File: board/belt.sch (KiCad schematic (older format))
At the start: 21 parts, among them J1 USB_B_Micro, J2 USB_B_Micro, J3 USB_B_Micro, J4 USB_B_Micro, P1 3352T-1-103LF, Q1 BSS138, Q2 BSS138, SW1 SW_DPDT, SW2 SW_Push, U1 Teensy4.0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

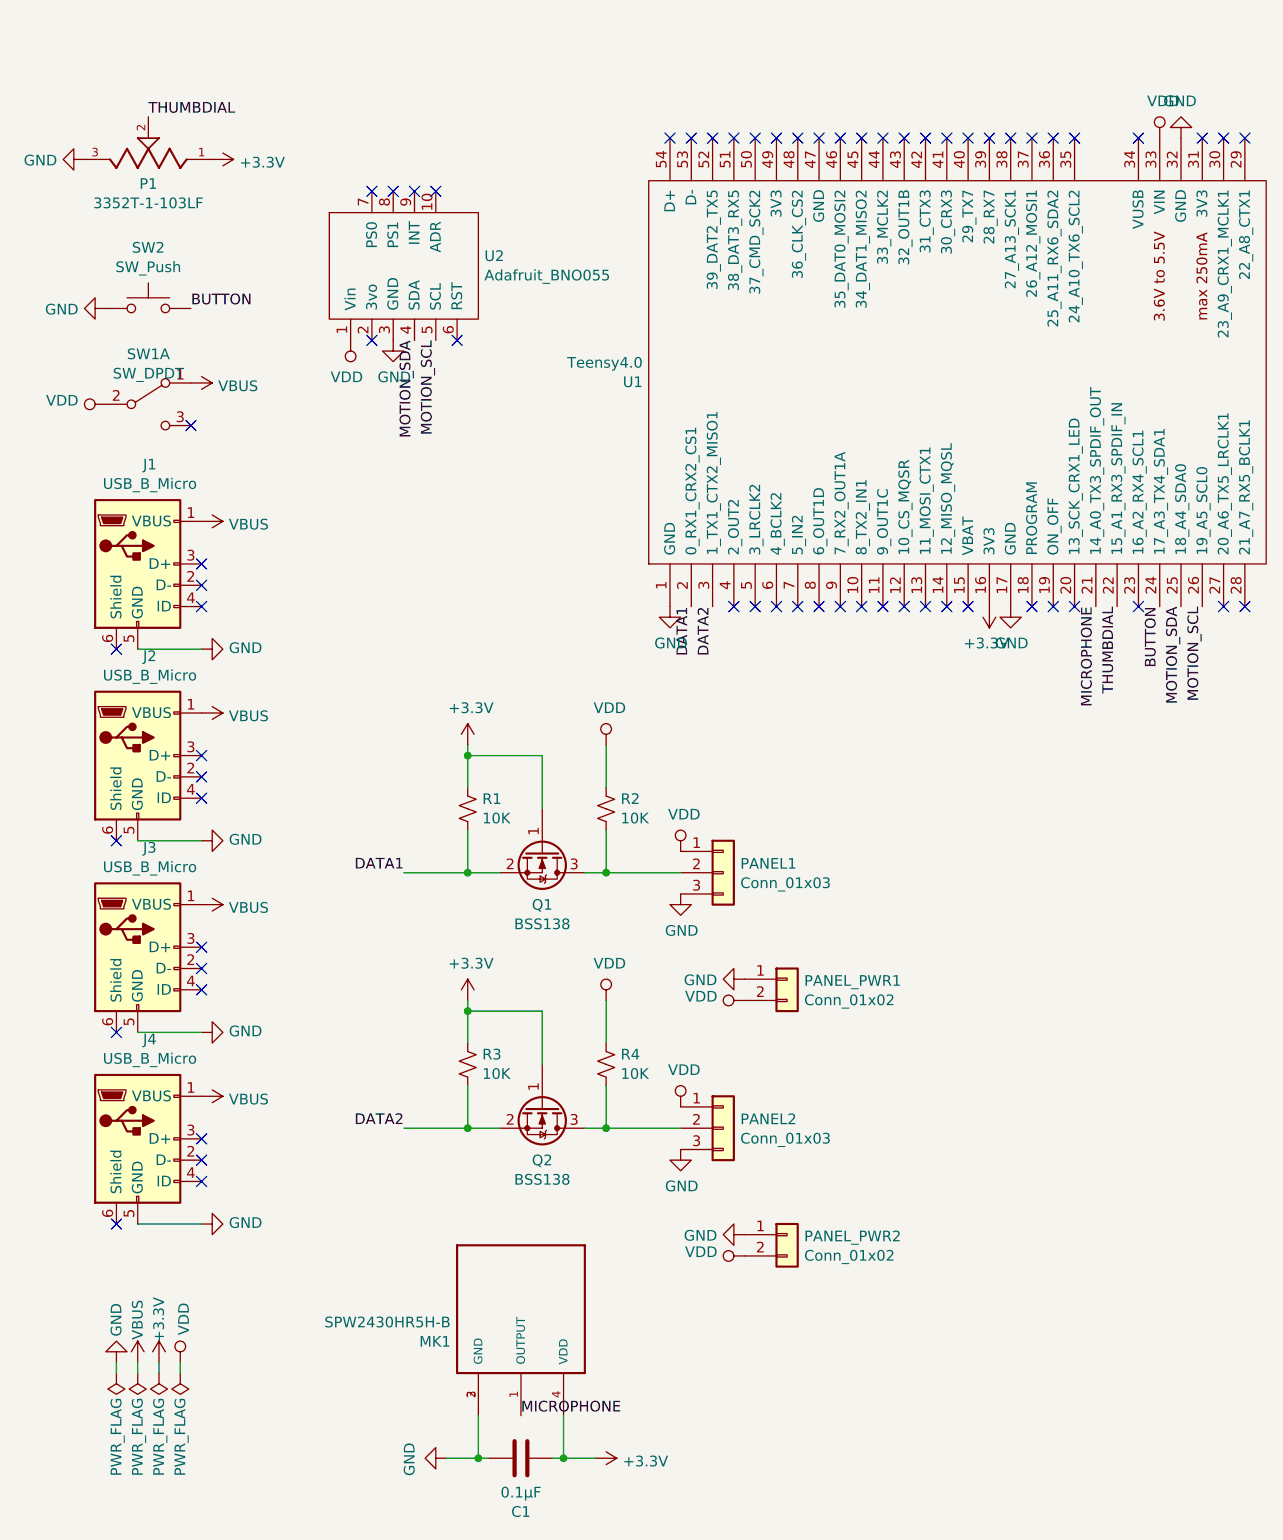
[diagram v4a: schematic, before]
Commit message: checkpoint for 3rd board layout with veritcal structure, two pots, and digital mic
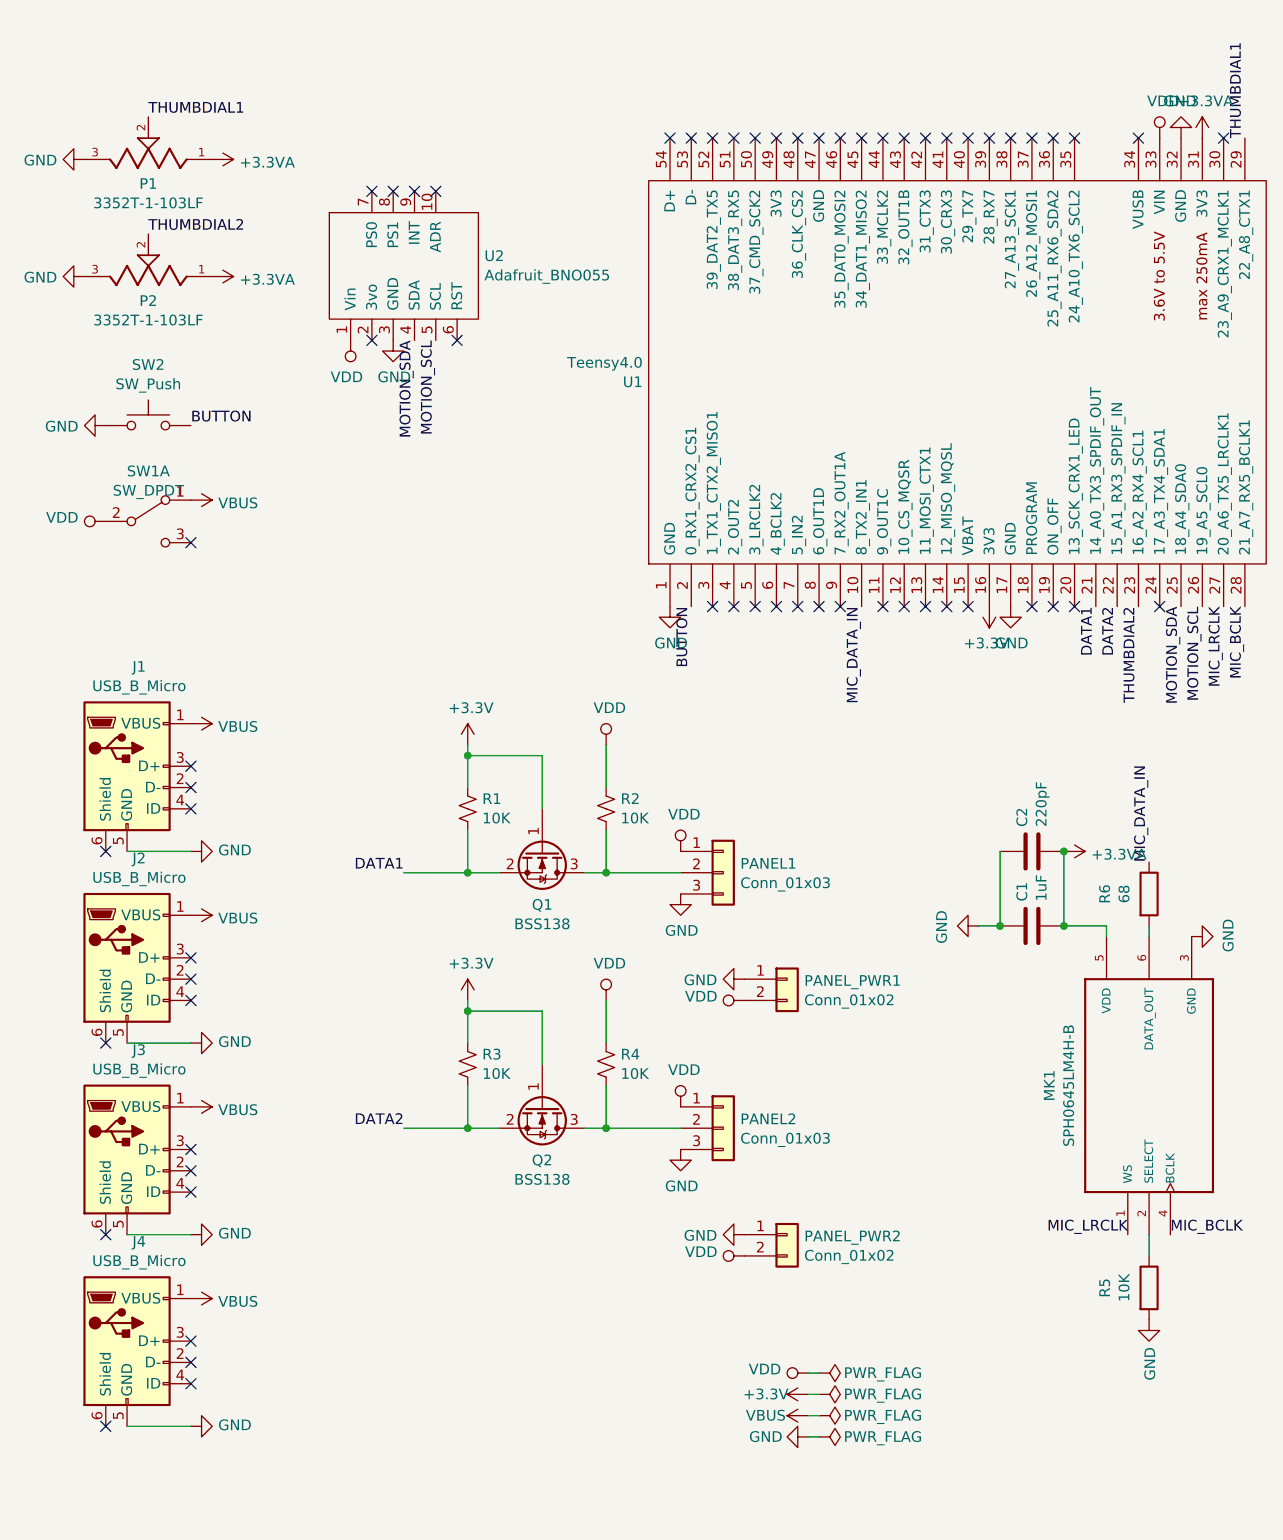
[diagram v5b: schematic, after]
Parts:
- removed MK1: SPW2430HR5H-B, SPW2430HR5H-B:MIC_SPW2430HR5H-B, symbol MIC_SPW2430HR5H-B:SPW2430HR5H-B
- added C2: 220pF, Capacitor_SMD:C_0805_2012Metric, symbol Device:C
- added MK1: SPH0645LM4H-B, Mic-SPH0645LM4H-B:MIC_SPH0645LM4H-B, symbol Mic_I2S_SPH0645LM4H-B:SPH0645LM4H-B
- added P2: 3352T-1-103LF, Potentiometer_THT:PDB12-H, symbol belt-rescue:3352T-1-103LF-3352T-1-103LF
- added R5: 10K, Resistor_SMD:R_0805_2012Metric, symbol Device:R
- added R6: 68, Resistor_SMD:R_0805_2012Metric, symbol Device:R
- C1: value 0.1µF -> 1uF
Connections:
- net MICROPHONE is gone; now on net DATA1: U1.21 (14_A0_TX3_SPDIF_OUT)
- net +3V3: no longer C1.1, P1.1 (CCW)
- net BUTTON: now also U1.2 (0_RX1_CRX2_CS1); no longer U1.24 (17_A3_TX4_SDA1)
- net DATA1: no longer U1.2 (0_RX1_CRX2_CS1)
- net DATA2: now also U1.22 (15_A1_RX3_SPDIF_IN); no longer U1.3 (1_TX1_CTX2_MISO1)
- net GND: now also C1.1, C2.1, MK1.3 (GND), P2.3 (CW), R5.2; no longer C1.2
- net MIC_DATA_IN: now reaches U1.10 (8_TX2_IN1)
- net MIC_DATA_IN: now also R6.1
- net THUMBDIAL2: now reaches U1.23 (16_A2_RX4_SCL1)
- net THUMBDIAL2: now also P2.2 (WIPER)
- net MIC_LRCLK: now reaches U1.27 (20_A6_TX5_LRCLK1)
- net MIC_LRCLK: now also MK1.1 (WS)
- net MIC_BCLK: now reaches U1.28 (21_A7_RX5_BCLK1)
- net MIC_BCLK: now also MK1.4 (BCLK)
- net THUMBDIAL1: now reaches U1.29 (22_A8_CTX1)
- net THUMBDIAL1: now also P1.2 (WIPER)
- net +3.3VA: now reaches U1.31 (3V3)
- net +3.3VA: now also C1.2, P1.1 (CCW), C2.2, MK1.5 (VDD), P2.1 (CCW)
- removed net THUMBDIAL: P1.2 (WIPER), U1.22 (15_A1_RX3_SPDIF_IN)
- new net: MK1.2 (SELECT), R5.1
- new net: MK1.6 (DATA_OUT), R6.2
- no-connect marks 65 -> 61
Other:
- moved on the sheet: J1, J2, J3, J4, SW1A, SW2

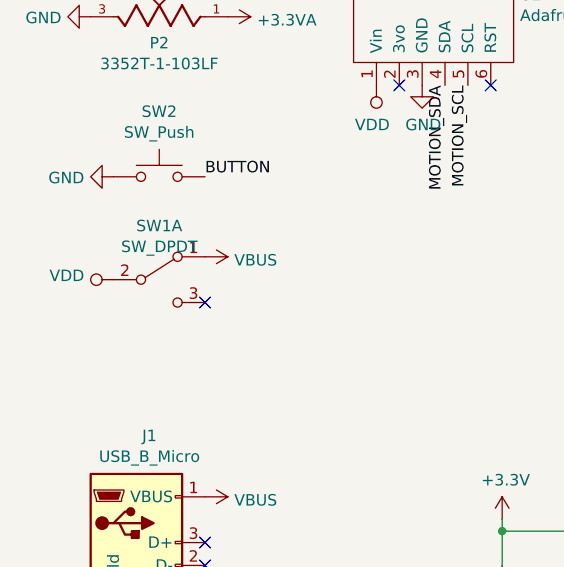
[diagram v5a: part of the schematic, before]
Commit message: new placement for led pads plus a strategy for securing them; tweaks; nearing final design
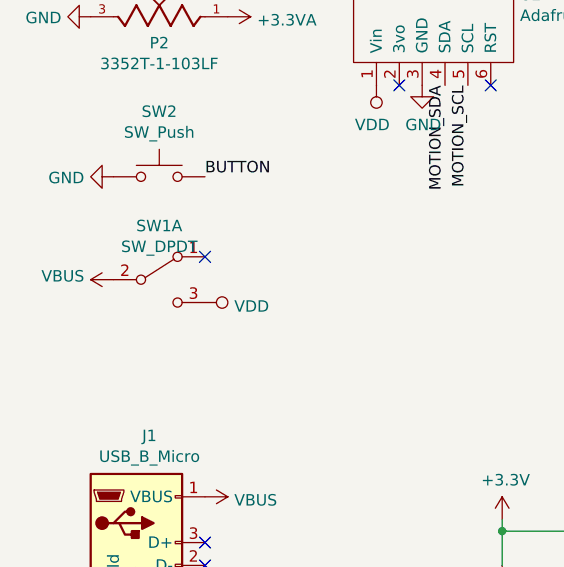
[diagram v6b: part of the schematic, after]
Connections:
- net VBUS: now also SW1.2 (B); no longer SW1.1 (A)
- net VDD: now also SW1.3 (C); no longer SW1.2 (B)
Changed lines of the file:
@@
 L power:VDD #PWR0120
 U 1 1 5E3ACFA6
+P 1700 2850
+F 0 "#PWR0120" H 1700 2700 50  0001 C CNN
+F 1 "VDD" V 1717 2978 50  0000 L CNN
+F 2 "" H 1700 2850 50  0001 C CNN
+F 3 "" H 1700 2850 50  0001 C CNN
+	1    1700 2850
+	0    1    1    0
+$EndComp
+$Comp
+L power:VBUS #PWR0111
+U 1 1 5E3E2BC8
 P 1300 2750
-F 0 "#PWR0120" H 1300 2600 50  0001 C CNN
-F 1 "VDD" V 1317 2878 50  0000 L CNN
+F 0 "#PWR0111" H 1300 2600 50  0001 C CNN
+F 1 "VBUS" V 1315 2878 50  0000 L CNN
 F 2 "" H 1300 2750 50  0001 C CNN
 F 3 "" H 1300 2750 50  0001 C CNN
 	1    1300 2750
 	0    -1   -1   0
-$EndComp
-$Comp
-L power:VBUS #PWR0111
-U 1 1 5E3E2BC8
-P 1700 2650
-F 0 "#PWR0111" H 1700 2500 50  0001 C CNN
-F 1 "VBUS" V 1715 2778 50  0000 L CNN
-F 2 "" H 1700 2650 50  0001 C CNN
-F 3 "" H 1700 2650 50  0001 C CNN
-	1    1700 2650
-	0    1    1    0
 $EndComp
 $Comp
@@
 $EndComp
 NoConn ~ 4250 3150
-NoConn ~ 1700 2850
+NoConn ~ 1700 2650
 $Comp
 L belt-rescue:3352T-1-103LF-3352T-1-103LF P2

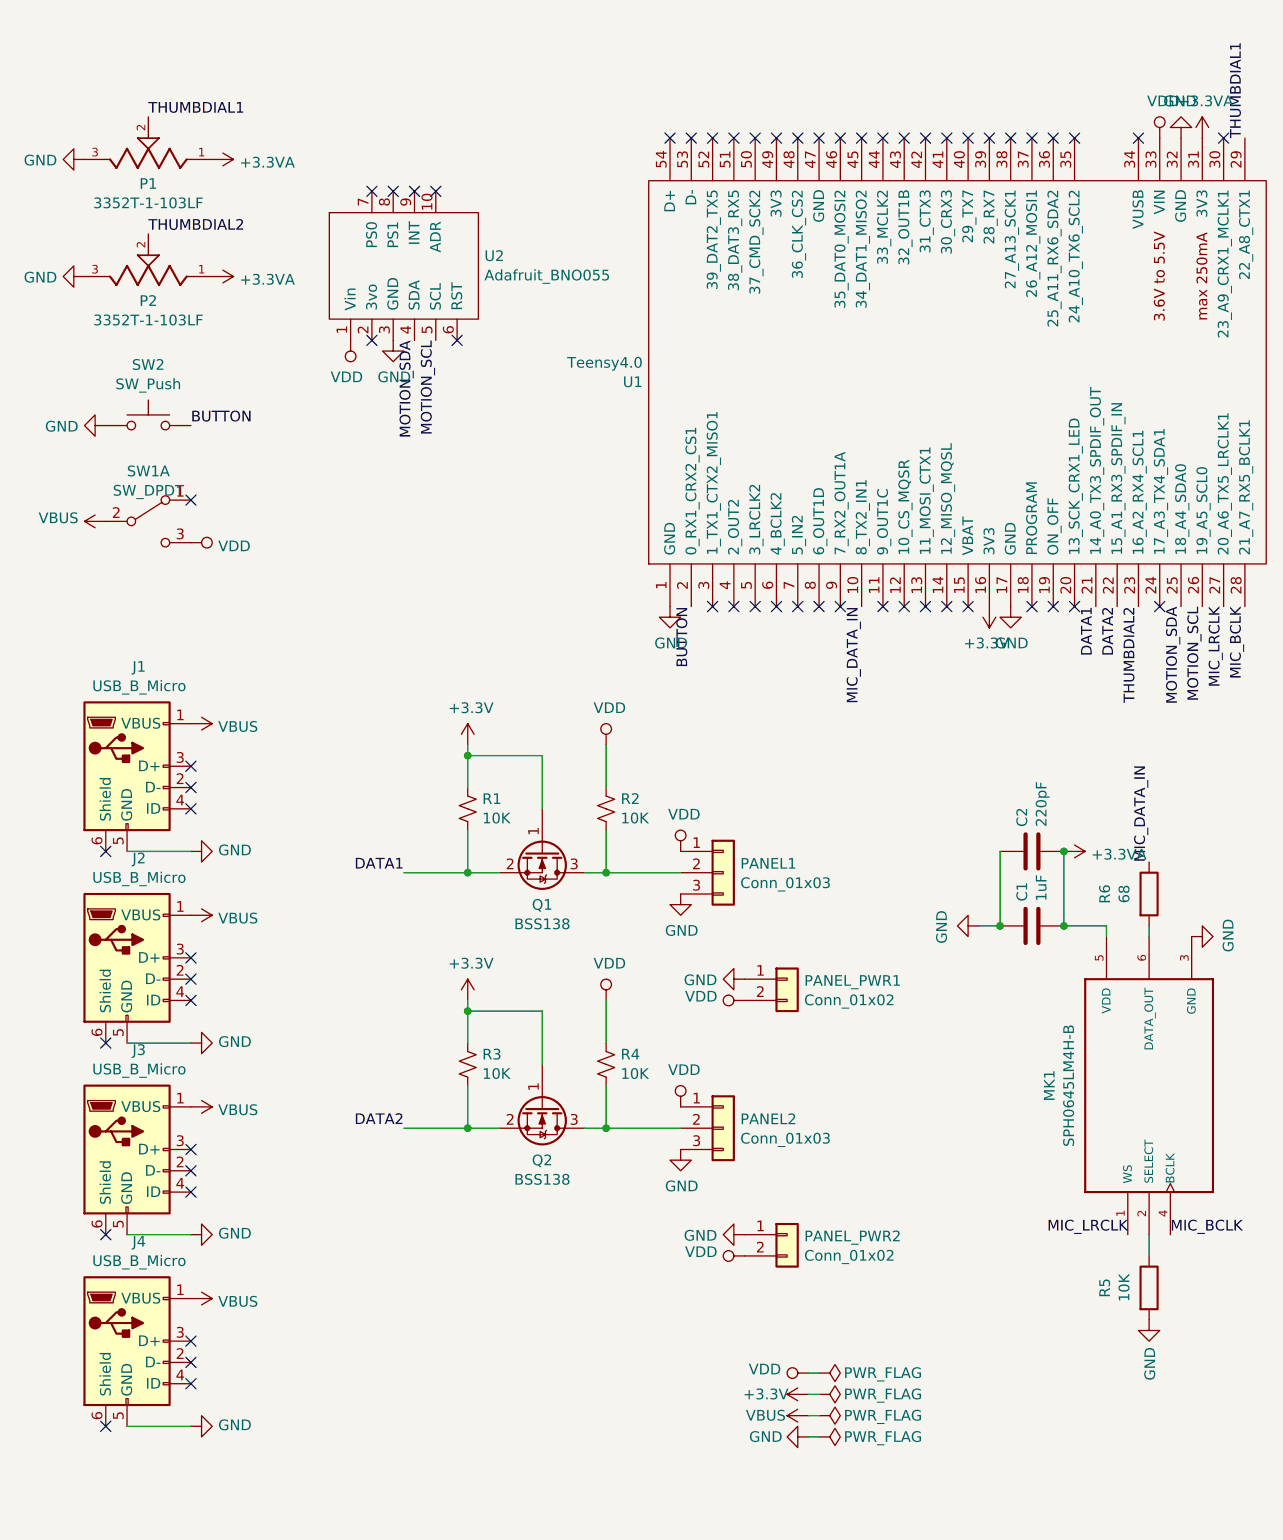
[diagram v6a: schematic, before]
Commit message: digikey was out of the DPDT switch I was going to use, so replace with a smaller (better?) one; shrink board vertically slightly in response
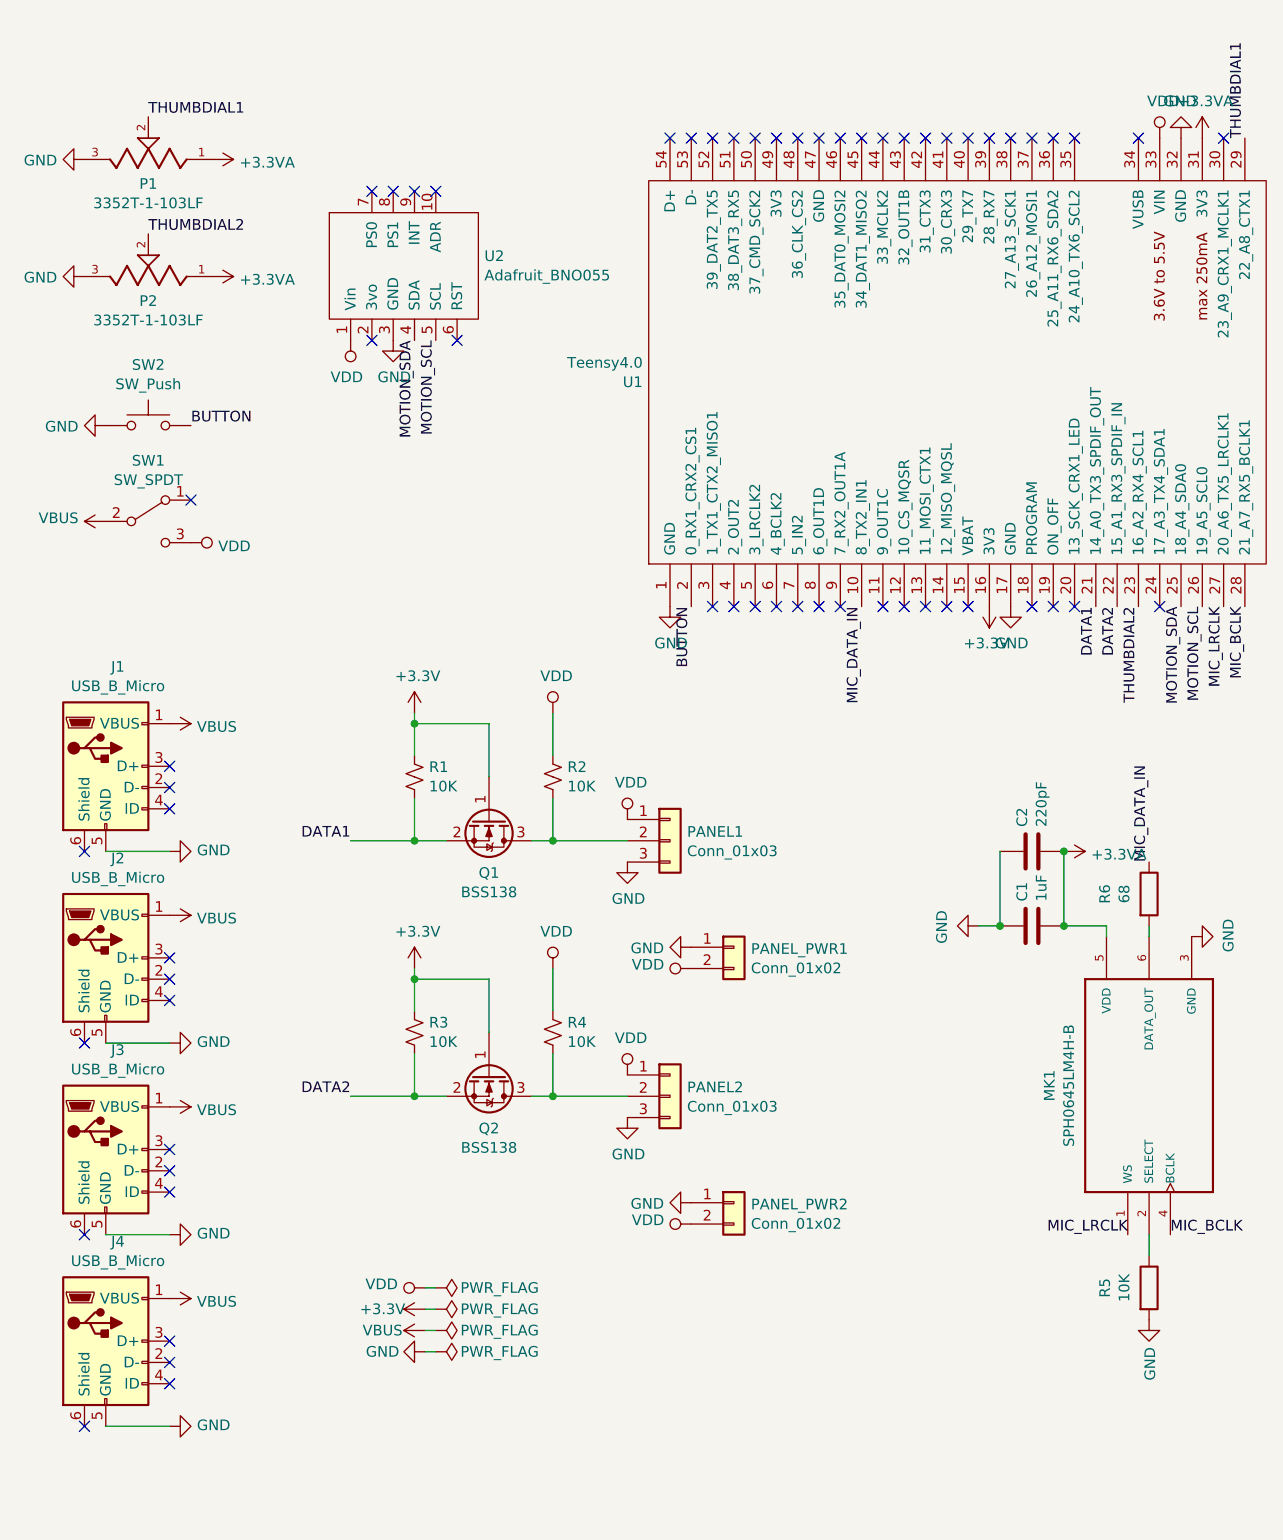
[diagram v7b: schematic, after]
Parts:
- removed SW1: SW_DPDT, engstad:slide-switch-MFS201N-9-Z, symbol Switch:SW_DPDT_x2
- added SW1: SW_SPDT, Extra SMD Components:Button_Switch_SPDT_GH36P010001, symbol Switch:SW_SPDT
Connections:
- net VBUS: now also SW1.2 (B)
- net VDD: now also SW1.3 (C)
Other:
- moved on the sheet: J1, J2, J3, J4, PANEL1, PANEL2, PANEL_PWR1, PANEL_PWR2, Q1, Q2, R1, R2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

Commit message: switch 10K resistors to 0603 package (being ambitious and buying in bulk); fix layout for new package
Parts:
- R1, R2, R3, R4, R5: footprint Resistor_SMD:R_0805_2012Metric -> Resistor_SMD:R_0603_1608Metric
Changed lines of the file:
@@
 F 0 "R1" H 2818 3996 50  0000 L CNN
 F 1 "10K" H 2818 3905 50  0000 L CNN
-F 2 "Resistor_SMD:R_0805_2012Metric" H 2750 3950 50  0001 C CNN
+F 2 "Resistor_SMD:R_0603_1608Metric" H 2750 3950 50  0001 C CNN
 F 3 "~" H 2750 3950 50  0001 C CNN
 	1    2750 3950
@@
 F 0 "R3" H 2818 5196 50  0000 L CNN
 F 1 "10K" H 2818 5105 50  0000 L CNN
-F 2 "Resistor_SMD:R_0805_2012Metric" H 2750 5150 50  0001 C CNN
+F 2 "Resistor_SMD:R_0603_1608Metric" H 2750 5150 50  0001 C CNN
 F 3 "~" H 2750 5150 50  0001 C CNN
 	1    2750 5150
@@
 F 0 "R4" H 3468 5196 50  0000 L CNN
 F 1 "10K" H 3468 5105 50  0000 L CNN
-F 2 "Resistor_SMD:R_0805_2012Metric" H 3400 5150 50  0001 C CNN
+F 2 "Resistor_SMD:R_0603_1608Metric" H 3400 5150 50  0001 C CNN
 F 3 "~" H 3400 5150 50  0001 C CNN
 	1    3400 5150
@@
 F 0 "R2" H 3468 3996 50  0000 L CNN
 F 1 "10K" H 3468 3905 50  0000 L CNN
-F 2 "Resistor_SMD:R_0805_2012Metric" H 3400 3950 50  0001 C CNN
+F 2 "Resistor_SMD:R_0603_1608Metric" H 3400 3950 50  0001 C CNN
 F 3 "~" H 3400 3950 50  0001 C CNN
 	1    3400 3950
@@
 F 0 "R5" V 5993 6350 50  0000 C CNN
 F 1 "10K" V 6084 6350 50  0000 C CNN
-F 2 "Resistor_SMD:R_0805_2012Metric" V 6130 6350 50  0001 C CNN
+F 2 "Resistor_SMD:R_0603_1608Metric" V 6130 6350 50  0001 C CNN
 F 3 "~" H 6200 6350 50  0001 C CNN
 	1    6200 6350
